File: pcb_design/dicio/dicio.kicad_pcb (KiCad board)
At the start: 2 copper layers, 93 x 93 mm, 88 parts, among them J1 USB_OTG, J2 Conn_01x06_Female, J3 Screw_Terminal_01x06, J4 Screw_Terminal_01x11, J5 Conn_02x03_Odd_Even, J6 Screw_Terminal_01x05, J7 Screw_Terminal_01x09, P1 USB_C_Plug_USB2.0, SW1 SW_SPST, SW2 SW_SPST, SW3 SW_DIP_x08, U1 FT232RL, U2 MCP2542FD, U3 dsPIC33EP512MC806, U4 TPS737, U5 PCA9670, U6 TPS61040, U7 RP604x, U8 gloxinia_connector_small, Y1 Crystal_GND24

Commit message: New dicio design.
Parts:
- removed C28: 10uF, Capacitor_SMD:C_1210_3225Metric
- removed D3, D5: LED, LED_SMD:LED_0603_1608Metric
- removed D6: MBR0530, Diode_SMD:D_SOD-123
- removed H1, H2, H3, H4: MountingHole, MountingHole:MountingHole_3.2mm_M3
- removed JP1: Jumper_NC_Small, Jumper:SolderJumper-2_P1.3mm_Open_RoundedPad1.0x1.5mm
- removed JP2: Jumper, Jumper:SolderJumper-2_P1.3mm_Open_RoundedPad1.0x1.5mm
- removed L1: 10uH, custom_footprints:L_6.5mmx4.5mm_Bourns
- removed L2: 2.2uH, custom_footprints:L_L4mm_D4mm_H1.8mm
- removed P1: USB_C_Plug_USB2.0, custom_footprints:USB_C_Receptacle_Amphenol_12401832E402A
- removed R16: 1.8M, Capacitor_SMD:C_0603_1608Metric
- removed R17: 205k, Capacitor_SMD:C_0603_1608Metric
- removed R21, R23: 4.9k, Resistor_SMD:R_0603_1608Metric
- removed SW3: SW_DIP_x08, Button_Switch_SMD:SW_DIP_SPSTx08_Slide_Omron_A6H-8101_W6.15mm_P1.27mm
- removed U8: gloxinia_connector_small, Connector_PinHeader_2.54mm:PinHeader_2x13_P2.54mm_Vertical
- added C29: 20pF, Capacitor_SMD:C_0603_1608Metric, F.Cu at (73.1, 75.2)
- added C30: 4.7nF, Capacitor_SMD:C_0603_1608Metric, F.Cu at (101.2, 53.7)
- added C31: 0.1uF, Capacitor_SMD:C_0603_1608Metric, F.Cu at (105.2, 82.8)
- added C32: 0.1uF, Capacitor_SMD:C_0603_1608Metric, F.Cu at (67.6, 85.5)
- added J8: USB_C_Receptacle, custom_footprints:USB_C_Receptacle_Amphenol_12401861XX12A, F.Cu at (107.5, 127.9)
- added Q1: Q_NMOS_GSD, Package_TO_SOT_SMD:SOT-23, F.Cu at (97.6, 54.5)
- added Y2: Crystal_GND24, Crystal:Crystal_SMD_Abracon_ABM3B-4Pin_5.0x3.2mm, F.Cu at (86.0, 72.3)
- C16: value 10uF -> 1uF; footprint Capacitor_SMD:C_1210_3225Metric -> Capacitor_SMD:C_0603_1608Metric
- C17: value 4.7pF -> 1uF
- C18: value 1uF -> 0.1uF; footprint Capacitor_SMD:C_1206_3216Metric -> Capacitor_SMD:C_0603_1608Metric
- C19, C27: value 10uF -> 0.1uF; footprint Capacitor_SMD:C_1210_3225Metric -> Capacitor_SMD:C_0603_1608Metric
- C20: value 10uF -> 1nF; footprint Capacitor_SMD:C_1210_3225Metric -> Capacitor_SMD:C_0603_1608Metric
- C21, C22: value 22uF -> 4.7uF; footprint Capacitor_SMD:C_1210_3225Metric -> Capacitor_SMD:C_1206_3216Metric
- C23: footprint Capacitor_SMD:C_1210_3225Metric -> Capacitor_SMD:C_1206_3216Metric
- C6: value 10uF -> 20pF; footprint Capacitor_SMD:C_1210_3225Metric -> Capacitor_SMD:C_0603_1608Metric
- C7, C8: value 10pF -> 20pF
- J1: value USB_OTG -> Conn_02x03_Counter_Clockwise; footprint Connector_USB:USB_Micro-B_Molex-105017-0001 -> Connector_PinSocket_2.54mm:PinSocket_2x03_P2.54mm_Vertical
- J3: value Screw_Terminal_01x06 -> USB_C_Receptacle; footprint custom_footprints:TB003-500-06 -> custom_footprints:USB_C_Receptacle_Amphenol_12401861XX12A
- J4: value Screw_Terminal_01x11 -> Micro_SD_Card; footprint custom_footprints:TB003-500-11 -> Connector_Card:microSD_HC_Wuerth_693072010801
- J5: value Conn_02x03_Odd_Even -> USB_C_Receptacle; footprint Connector_PinHeader_2.54mm:PinHeader_2x03_P2.54mm_Vertical -> custom_footprints:USB_C_Receptacle_Amphenol_12401861XX12A
- J6: value Screw_Terminal_01x05 -> USB_C_Receptacle; footprint custom_footprints:TB003-500-05 -> custom_footprints:USB_C_Receptacle_Amphenol_12401861XX12A
- J7: value Screw_Terminal_01x09 -> Conn_02x13_Odd_Even; footprint custom_footprints:TB003-500-06 -> Connector_PinHeader_2.54mm:PinHeader_2x13_P2.54mm_Vertical
- N1: footprint custom_footprints:Enclosure-Hammond-1554LA -> custom_footprints:Enclosure-Gloxinia2
- R1: value 10k -> 1k
- R11: value 120 -> 1M
- R18: value 120R -> 60R; footprint Resistor_THT:R_Axial_DIN0204_L3.6mm_D1.6mm_P7.62mm_Horizontal -> Resistor_SMD:R_0603_1608Metric
- R4, R9: value 750 -> 100k
- R7: value 1M -> 60R
- SW1, SW2: footprint Button_Switch_SMD:SW_SPST_KMR2 -> Button_Switch_SMD:SW_Push_1P1T_NO_CK_KMR2
- U1: value FT232RL -> dsPIC33EP256MU806; footprint Package_SO:SSOP-28_5.3x10.2mm_P0.65mm -> Package_QFP:TQFP-64_10x10mm_P0.5mm
- U3: value dsPIC33EP512MC806 -> S70FL01GS; footprint Package_QFP:TQFP-64_10x10mm_P0.5mm -> custom_footprints:SOIC-16_25.75x18.75mm_P2.5mm; moved to B.Cu
- U5: value PCA9670 -> SiP32431; footprint Package_SO:TSSOP-16_4.4x5mm_P0.65mm -> Package_TO_SOT_SMD:SOT-363_SC-70-6
- U6: value TPS61040 -> SiP32431; footprint Package_TO_SOT_SMD:SOT-23-5 -> Package_TO_SOT_SMD:SOT-363_SC-70-6
- U7: value RP604x -> ADM7170; footprint custom_footprints:DFN_12_Pin_2.7x3mm_P0.5mm -> Package_CSP:LFCSP-8-1EP_3x3mm_P0.5mm_EP1.45x1.74mm
- moved J7 85.2 mm to (70.0, 45.0), turned to 90 degrees
- moved J3 84.9 mm to (62.5, 127.9)
- moved C4 80.4 mm to (52.0, 50.8), turned to 90 degrees
- moved R6 79.9 mm to (51.3, 53.5)
- moved SW2 78.0 mm to (56.0, 50.8), turned to 0 degrees
- moved J2 70.1 mm to (55.0, 56.0)
- moved R2 65.7 mm to (61.2, 51.0), turned to -90 degrees
- moved C3 64.8 mm to (62.9, 50.9), turned to 90 degrees
- moved SW1 63.0 mm to (66.6, 51.0), turned to 0 degrees
- moved U5 59.6 mm to (119.5, 96.8)
- moved J6 56.6 mm to (77.5, 127.9), turned to 0 degrees
- moved R7 55.2 mm to (99.4, 49.5), turned to 0 degrees
- moved R4 54.3 mm to (69.6, 75.5), turned to 0 degrees
- moved R12 52.6 mm to (106.7, 76.2)
- moved R18 50.4 mm to (99.4, 51.1), turned to 180 degrees
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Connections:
- net /~MCLR renamed /~{MCLR}
- C12 pad 1: +3V3 -> GND
- C12 pad 2: GND -> +3V3
- C13 pad 2: +3V3 -> VDDA
- C14 pad 1: +3V3 -> GND
- C14 pad 2: GND -> +3V3
- C16 pad 1: VBUS -> +3V3
- C17 pad 1: +12V -> VDDA
- C17 pad 2: Net-(C17-Pad2) -> GND
- C18 pad 1: +12V -> /S_PS
- C19 pad 1: VBUS -> /S_PS
- C2 pad 1: GND -> +3V3
- C2 pad 2: Net-(C2-Pad2) -> GND
- C20 pad 1: VBUS -> Net-(C20-Pad1)
- C21 pad 1: +5V -> VDDA
- C22 pad 1: +5V -> VBUS
- C23 pad 1: +3V3 -> /VCAP
- C27 pad 1: +12V -> +3V3
- C3 pad 1: Net-(C3-Pad1) -> /BTN
- C6 pad 1: Net-(C6-Pad1) -> GND
- C6 pad 2: GND -> /SOSC1
- C7 pad 2: Net-(C7-Pad2) -> /OSC2
- C8 pad 2: /CLK_IN -> /OSC1
- J1 pad 1: /V_USBC -> +3V3
- J1 pad 2: /D- -> /U1RX
- J1 pad 3: /D+ -> /~{U1RTS}
- J1 pad 4: Net-(J1-Pad4) -> /~{U1CTS}
- J1 pad 5: GND -> /U1TX
- J2 pad 6: /PGM -> unconnected-(J2-Pad6)
- J4 pad 1: GND -> unconnected-(J4-Pad1)
- J4 pad 2: /SCK2 -> /~{CS_SD}
- J4 pad 3: /SDO2 -> /MOSI1
- J4 pad 4: /SDI2 -> +3V3
- J4 pad 5: /~CS2_1 -> /SCK1
- J4 pad 6: /~CS2_2 -> GND
- J4 pad 7: +3V3 -> /MISO1
- J4 pad 8: /~INT2 -> unconnected-(J4-Pad8)
- J4 pad 9: /SDA2 -> GND
- J7 pad 1: +3V3 -> VBUS
- J7 pad 2: /U1RX -> VBUS
- J7 pad 3: /U1TX -> /V_USBC
- J7 pad 4: /~U1RTS -> VBUS
- J7 pad 5: /~U1CTS -> /CAN_H
- J7 pad 6: GND -> /V_USBC
- R1 pad 1: /~RST_FTDI -> Net-(Q1-Pad1)
- R1 pad 2: VBUS -> /TERM
- R10 pad 1: Net-(R10-Pad1) -> /~{MCLR_w}
- R11 pad 1: /CAN_L -> /OSC2
- R11 pad 2: /CAN_H -> /OSC1
- R18 pad 1: /CAN_L -> Net-(C30-Pad1)
- R18 pad 2: /CAN_H -> Net-(Q1-Pad2)
- R19 pad 1: Net-(P1-PadA5) -> /VCONN
- R2 pad 2: Net-(C3-Pad1) -> /BTN
- R20 pad 2: Net-(P1-PadB5) -> /CC1
- R22 pad 2: /~INT1 -> /~{INT1}
- R24 pad 2: /~INT2 -> /~{INT2}
- R4 pad 1: /BLINK -> +3V3
- R4 pad 2: Net-(D3-Pad2) -> /~{SQICS1}
- R7 pad 1: Net-(C7-Pad2) -> /CAN_L
- R7 pad 2: /CLK_IN -> Net-(C30-Pad1)
- R9 pad 1: Net-(R9-Pad1) -> +3V3
- R9 pad 2: Net-(D5-Pad2) -> /~{SQICS0}
- SW1 pad 2: Net-(C3-Pad1) -> /BTN
- U1 pad 1: /MCU_RXD -> /~{U1RTS}
- U1 pad 10: Net-(U1-Pad10) -> +3V3
- U1 pad 11: /MCU_~RTS -> /S_PS_SW
- U1 pad 12: Net-(U1-Pad12) -> /~{INT1}
- U1 pad 13: Net-(U1-Pad13) -> /OW2
- U1 pad 14: Net-(U1-Pad14) -> /AS2
- U1 pad 15: /D+ -> /OW4
- U1 pad 16: /D- -> /AS4
- U1 pad 17: Net-(C2-Pad2) -> /PGC
- U1 pad 18: GND -> /PGD
- U1 pad 19: /~RST_FTDI -> VDDA
- U1 pad 2: Net-(U1-Pad2) -> /OW1
- U1 pad 20: +5V -> GND
- U1 pad 21: GND -> /EN_VA
- U1 pad 22: Net-(U1-Pad22) -> /SYNC
- U1 pad 23: Net-(R9-Pad1) -> /CAN_C2
- U1 pad 24: (no net) -> /CAN_C1
- U1 pad 26: GND -> +3V3
- U1 pad 27: Net-(U1-Pad27) -> /C1TX
- U1 pad 28: Net-(U1-Pad28) -> /C1RX
- U1 pad 3: /MCU_~CTS -> /U1TX
- U1 pad 4: +3V3 -> /OW3
- U1 pad 5: /MCU_TXD -> /~{U1CTS}
- U1 pad 6: Net-(U1-Pad6) -> /U1RX
- U1 pad 7: GND -> /~{MCLR_w}
- U1 pad 8: (no net) -> unconnected-(U1-Pad8)
- U1 pad 9: Net-(U1-Pad9) -> GND
- U3 pad 1: /MCU_~RTS -> /~{HOLD}
- U3 pad 10: +3V3 -> GND
- U3 pad 11: /BLINK -> unconnected-(U3-Pad11)
- U3 pad 12: /ERR -> unconnected-(U3-Pad12)
- U3 pad 13: Net-(U3-Pad13) -> unconnected-(U3-Pad13)
- U3 pad 14: Net-(U3-Pad14) -> +3V3
- U3 pad 15: Net-(U3-Pad15) -> /SI
- U3 pad 16: Net-(U3-Pad16) -> /SQICLK
- U3 pad 2: /MCU_~CTS -> +3V3
- U3 pad 3: /MCU_TXD -> /~{RESET_M}
- U3 pad 4: /SDO2 -> unconnected-(U3-Pad4)
- U3 pad 5: /MCU_RXD -> unconnected-(U3-Pad5)
- U3 pad 6: /SCK2 -> /~{SQICS1}
- U3 pad 7: Net-(R10-Pad1) -> /~{SQICS0}
- U3 pad 8: Net-(U3-Pad8) -> /SO
- U3 pad 9: GND -> /~{WP}
- U5 pad 1: +3V3 -> /S_PS
- U5 pad 2: +3V3 -> GND
- U5 pad 3: +3V3 -> /S_PS_SW
- U5 pad 4: Net-(SW3-Pad16) -> +3V3
- U5 pad 5: Net-(SW3-Pad15) -> GND
- U5 pad 6: Net-(SW3-Pad14) -> unconnected-(U5-Pad6)
- U6 pad 1: Net-(D6-Pad2) -> /S_PS
- U6 pad 3: Net-(C17-Pad2) -> /EN_VA
- U6 pad 4: VBUS -> VDDA
- U6 pad 5: VBUS -> GND
- U7 pad 1: VBUS -> VDDA
- U7 pad 2: VBUS -> VDDA
- U7 pad 3: GND -> VDDA
- U7 pad 4: GND -> Net-(C20-Pad1)
- U7 pad 5: GND -> /EN_VA
- U7 pad 6: +5V -> GND
- U7 pad 7: +5V -> VBUS
- U7 pad 8: Net-(L2-Pad2) -> VBUS
- Y1 pad 1: /CLK_IN -> /SOSC2
- Y1 pad 3: Net-(C7-Pad2) -> /SOSC1
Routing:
- net +3V3: track 606.6 -> 342.9 mm, vias 29 -> 18
- net +5V: track 190.2 -> 0.00 mm, vias 2 -> 0
- net /S_PS: track 0.00 -> 144.3 mm, vias 0 -> 6
- net +12V: track 130.5 -> 0.00 mm, vias 4 -> 0
- net /~{INT1}: track 0.00 -> 121.3 mm, vias 0 -> 6
- net /~{MCLR}: track 134.0 -> 12.8 mm, vias 12 -> 0
- net /~{U1CTS}: track 0.00 -> 107.3 mm, vias 0 -> 4
- net /CLK: track 104.0 -> 0.00 mm, vias 4 -> 0
- net /~{U1RTS}: track 0.00 -> 98.7 mm, vias 0 -> 4
- net /~{INT2}: track 0.00 -> 96.3 mm, vias 0 -> 8
- net /~INT2: track 96.2 -> 0.00 mm, vias 4 -> 0
- net /~RST2: track 88.7 -> 0.00 mm, vias 1 -> 0
- net /U1RX: track 58.7 -> 136.8 mm
- net /~U1RTS: track 71.0 -> 0.00 mm
- net /SDA2: track 79.4 -> 150.2 mm, vias 3 -> 10
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- added copper zone on F.Cu, net /S_PS
- removed copper zone on F.Cu, net +5V
- removed copper zone on F.Cu, net VBUS
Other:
- outline, holes or cut-outs redrawn
- net class Default removed
- board text removed: "12V"
- board text removed: "3.3V"
- board text removed: "5V"
- board text removed: "ACT"
- board text removed: "ADDR"
- board text removed: "BLK"
- board text removed: "BP"
- board text removed: "CH"
- board text removed: "CL"
- board text removed: "CLK"
- board text removed: "CLK IN"
- board text removed: "ERR"
- board text removed: "G IO"
- board text removed: "GND"
- board text removed: "IO"
- board text removed: "PGM"
- board text removed: "PWR"
- board text removed: "RST"
- board text removed: "RX"
- board text removed: "Rev. 4"
- board text removed: "SCK"
- board text removed: "SCL"
- board text removed: "SDA"
- board text removed: "SDI"
- board text removed: "SDO"
- board text removed: "TERM"
- board text removed: "TX"
- board text removed: "USER"
- board text removed: "VB"
- board text removed: "dicio"
- board text removed: "gloxinia system"
- board text removed: "~CS1"
- board text removed: "~CS2"
- board text removed: "~CTS"
- board text removed: "~INT"
- board text removed: "~RST"
- board text removed: "~RTS"

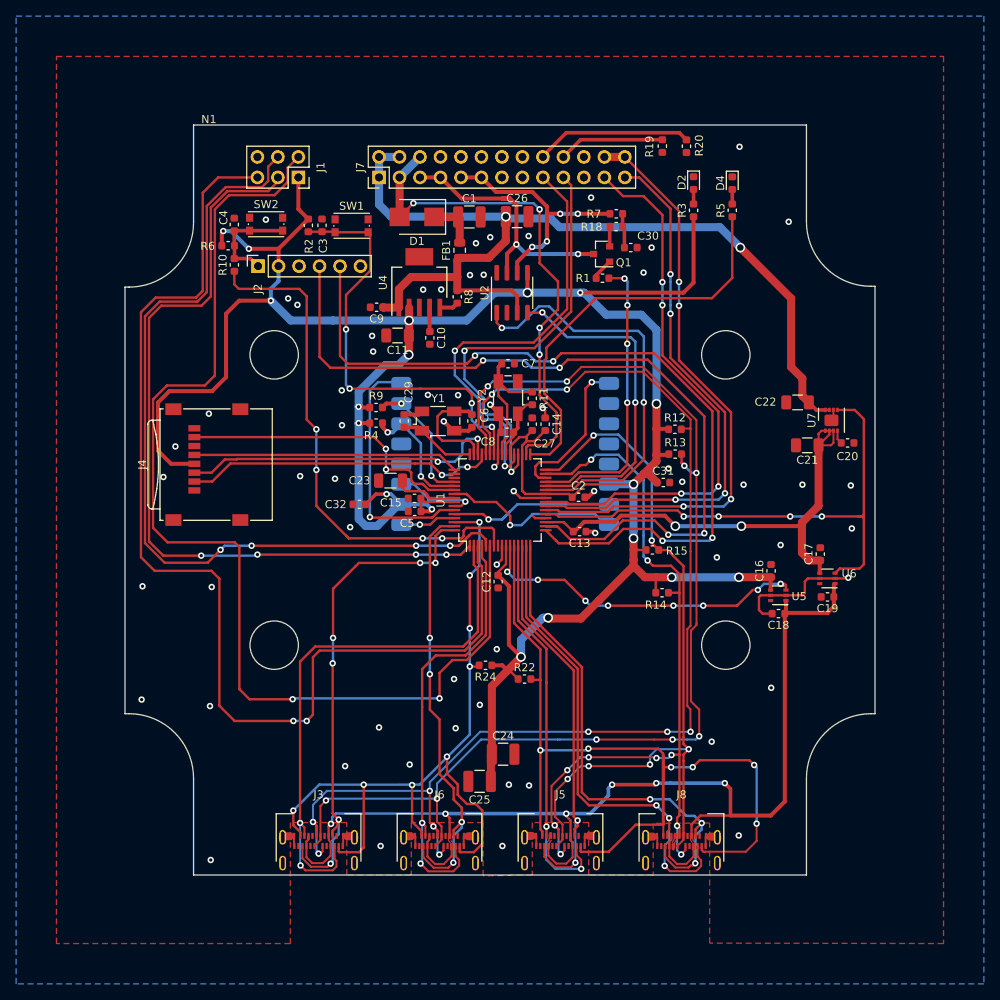
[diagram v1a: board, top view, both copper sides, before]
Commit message: Updated for new mounting hole locations
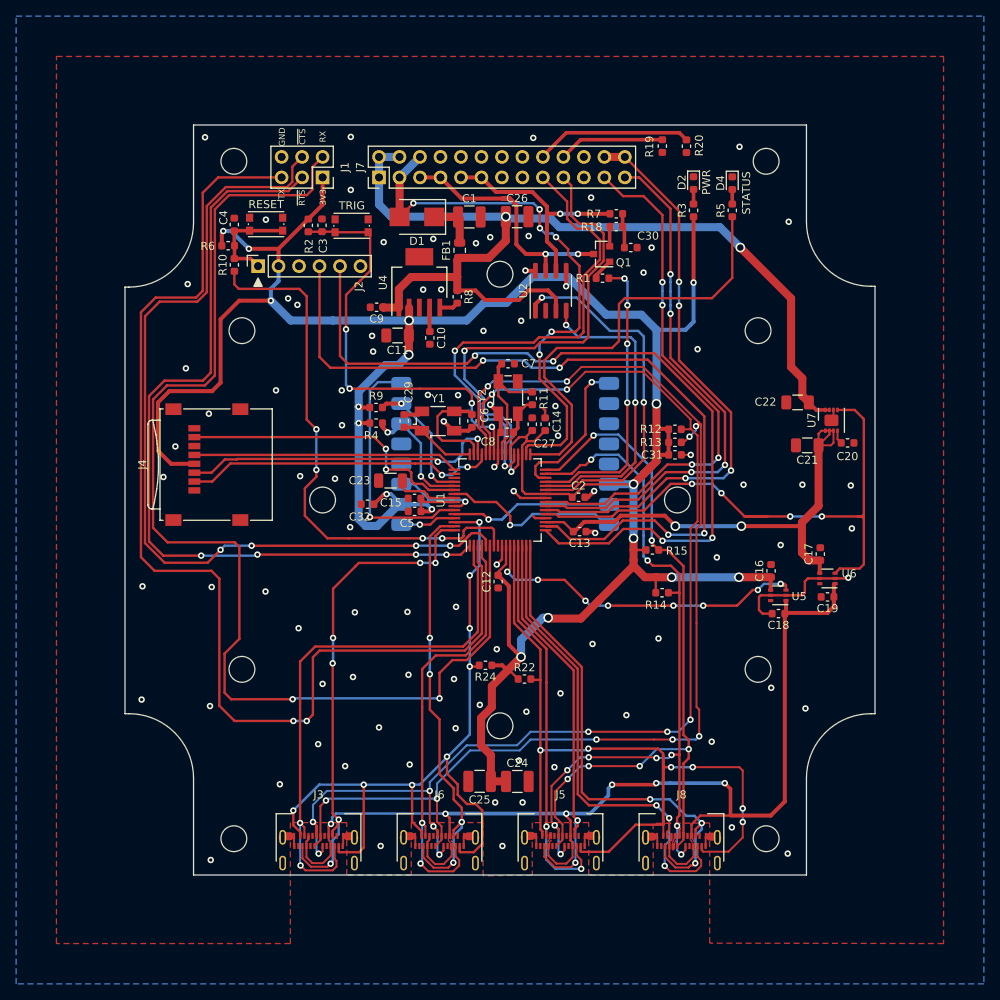
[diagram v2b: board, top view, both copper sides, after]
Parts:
- moved U2 4.81 mm to (91.3, 59.0)
- moved C24 3.81 mm to (87.2, 119.9)
- moved C31 3.72 mm to (106.7, 79.4)
- moved J1 3.00 mm to (63.0, 45.0)
- moved R13 1.46 mm to (106.7, 77.8)
- moved C32 1.02 mm to (68.6, 85.5)
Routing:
- net /D-: track 53.2 -> 60.7 mm
- net /D+: track 54.0 -> 61.1 mm
- net /V_USBC: track 63.0 -> 69.5 mm, vias 4 -> 6
- net /U1RX: track 136.8 -> 143.2 mm
- net /C1TX: track 51.4 -> 45.6 mm
- net /EN_VA: track 66.8 -> 72.4 mm
- net VBUS: track 116.8 -> 122.1 mm
- net /~{INT1}: track 121.3 -> 116.7 mm
- net /C1RX: track 42.4 -> 38.5 mm
- net /ERR: track 51.4 -> 55.1 mm
- net /~{U1CTS}: track 107.3 -> 110.4 mm
- net /U1TX: track 138.5 -> 141.5 mm
- net /~{U1RTS}: track 98.7 -> 101.2 mm
- net GND: track 65.4 -> 67.8 mm, vias 63 -> 93
- net /~{MCLR_w}: track 64.8 -> 67.1 mm
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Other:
- board text added: "3V3"
- board text added: "GND"
- board text added: "PWR"
- board text added: "RESET"
- board text added: "RX"
- board text added: "STATUS"
- board text added: "TRIG"
- board text added: "TX"
- board text added: "~{CTS}"
- board text added: "~{RTS}"

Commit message: Improved design.
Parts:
- moved C31 2.00 mm to (106.7, 77.4)
- moved R12 2.00 mm to (106.7, 74.2)
- moved R13 2.00 mm to (106.7, 75.8)
- moved SW2 1.30 mm to (57.3, 50.8)
- moved D4 0.50 mm to (113.3, 45.7)
- moved R5 0.50 mm to (113.3, 49.1)
- moved C4 0.45 mm to (51.6, 50.9), turned to 0 degrees
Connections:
- U1 pad 27: /C1TX -> unconnected-(U1-Pad27)
- U1 pad 3: /U1TX -> /OW3
- U1 pad 4: /OW3 -> /U1TX
- U1 pad 51: unconnected-(U1-Pad51) -> /C1TX
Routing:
- net /C1TX: track 45.6 -> 55.7 mm
- net /U1TX: track 141.5 -> 147.8 mm, vias 2 -> 4
- net /S_PS: track 144.3 -> 139.2 mm, vias 6 -> 7
- net /~{U1CTS}: track 110.4 -> 114.4 mm, vias 4 -> 6
- net /U1RX: track 143.2 -> 146.6 mm
- net /EN_VA: track 72.4 -> 75.7 mm
- net /~{MCLR}: track 12.8 -> 16.1 mm
- net /SYNC: track 72.1 -> 75.0 mm
- net /CAN_C2: track 66.4 -> 69.3 mm
- net /CAN_C1: track 66.0 -> 68.9 mm
- net /~{MCLR_w}: track 67.1 -> 69.5 mm
- net /TERM: track 36.2 -> 34.3 mm
- net /C1RX: track 38.5 -> 36.6 mm
- net /PGC: track 100.6 -> 102.0 mm
- net GND: track 67.8 -> 66.6 mm, vias 93 -> 92
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
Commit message: Placement update.
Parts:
- moved D2 98.9 mm to (56.1, 129.3), turned to 90 degrees
- moved R3 88.7 mm to (56.1, 120.3), turned to -90 degrees
- moved D4 83.8 mm to (113.9, 129.5), turned to 90 degrees
- moved R5 67.2 mm to (114.1, 116.3), turned to -90 degrees
- moved J4 3.21 mm to (50.8, 78.2), turned to 180 degrees
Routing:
- net /ERR: track 55.1 -> 92.7 mm, vias 0 -> 2
- net +3V3: track 343.8 -> 362.0 mm, vias 18 -> 21
- net Net-(D4-Pad2): track 1.80 -> 13.3 mm
- net Net-(D2-Pad2): track 1.81 -> 7.41 mm
- net /~{CS_SD}: track 38.7 -> 34.5 mm
- net /MISO1: track 37.3 -> 41.5 mm
- net /SYNC: track 75.0 -> 72.6 mm, vias 4 -> 2
- net /MOSI1: track 40.3 -> 38.0 mm
- net /CAN_C2: track 69.3 -> 67.2 mm, vias 4 -> 2
- net /CAN_C1: track 68.9 -> 67.1 mm, vias 4 -> 2
- net /~{INT2}: track 96.3 -> 97.4 mm
- net /SCK1: track 33.0 -> 33.9 mm
- net GND: vias 92 -> 95
- net /TERM: vias 4 -> 2

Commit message: Update.
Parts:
- added C28: 0.1uF, Capacitor_SMD:C_0603_1608Metric, F.Cu at (112.5, 64.5)
- added R16: 10k, Capacitor_SMD:C_0603_1608Metric, F.Cu at (112.5, 61.4)
- added U8: FT232RL, Package_SO:SSOP-28_5.3x10.2mm_P0.65mm, F.Cu at (106.7, 60.2)
- U1: value dsPIC33EP256MU806 -> dsPIC33EP512MC806
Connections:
- C11 pad 1: +3V3 -> +3.3V
- C12 pad 2: +3V3 -> +3.3V
- C14 pad 2: +3V3 -> +3.3V
- C15 pad 1: +3V3 -> +3.3V
- C16 pad 1: +3V3 -> +3.3V
- C2 pad 1: +3V3 -> +3.3V
- C24 pad 1: +3V3 -> +3.3V
- C25 pad 1: +3V3 -> +3.3V
- C27 pad 1: +3V3 -> +3.3V
- C31 pad 1: +3V3 -> +3.3V
- C32 pad 1: +3V3 -> +3.3V
- C5 pad 1: +3V3 -> +3.3V
- J1 pad 1: +3V3 -> +3.3V
- J2 pad 2: +3V3 -> +3.3V
- J3 pad A10: /AS1 -> /SCL2
- J3 pad A3: /OW1 -> /SDA2
- J3 pad A6: /SDA2 -> /OW1
- J3 pad A7: /SCL2 -> /AS1
- J3 pad B10: /AS1 -> /SCL2
- J3 pad B3: /OW1 -> /SDA2
- J3 pad B6: /SDA2 -> /OW1
- J3 pad B7: /SCL2 -> /AS1
- J4 pad 4: +3V3 -> +3.3V
- J5 pad A10: /AS2 -> /SCL1
- J5 pad A3: /OW2 -> /SDA1
- J5 pad A6: /SDA1 -> /OW2
- J5 pad A7: /SCL1 -> /AS2
- J5 pad B10: /AS2 -> /SCL1
- J5 pad B3: /OW2 -> /SDA1
- J5 pad B6: /SDA1 -> /OW2
- J5 pad B7: /SCL1 -> /AS2
- J6 pad A10: /AS3 -> /SCL2
- J6 pad A3: /OW3 -> /SDA2
- J6 pad A6: /SDA2 -> /OW3
- J6 pad A7: /SCL2 -> /AS3
- J6 pad B10: /AS3 -> /SCL2
- J6 pad B3: /OW3 -> /SDA2
- J6 pad B6: /SDA2 -> /OW3
- J6 pad B7: /SCL2 -> /AS3
- J8 pad A10: /AS4 -> /SCL1
- J8 pad A3: /OW4 -> /SDA1
- J8 pad A6: /SDA1 -> /OW4
- J8 pad A7: /SCL1 -> /AS4
- J8 pad B10: /AS4 -> /SCL1
- J8 pad B3: /OW4 -> /SDA1
- J8 pad B6: /SDA1 -> /OW4
- J8 pad B7: /SCL1 -> /AS4
- R12 pad 1: +3V3 -> +3.3V
- R13 pad 1: +3V3 -> +3.3V
- R14 pad 1: +3V3 -> +3.3V
- R15 pad 1: +3V3 -> +3.3V
- R2 pad 1: +3V3 -> +3.3V
- R22 pad 1: +3V3 -> +3.3V
- R24 pad 1: +3V3 -> +3.3V
- R3 pad 1: +3V3 -> +3.3V
- R4 pad 1: +3V3 -> +3.3V
- R6 pad 1: +3V3 -> +3.3V
- R9 pad 1: +3V3 -> +3.3V
- U1 pad 10: +3V3 -> +3.3V
- U1 pad 26: +3V3 -> +3.3V
- U1 pad 27: unconnected-(U1-Pad27) -> /USB_CTS
- U1 pad 33: /ERR -> /USB_RX
- U1 pad 34: /V_USBC -> /USB_TX
- U1 pad 35: +3V3 -> /USB_RTS
- U1 pad 36: /D- -> /ERR
- U1 pad 37: /D+ -> unconnected-(U1-Pad37)
- U1 pad 38: +3V3 -> +3.3V
- U1 pad 57: +3V3 -> +3.3V
- U2 pad 5: +3V3 -> +3.3V
- U3 pad 14: +3V3 -> +3.3V
- U3 pad 2: +3V3 -> +3.3V
- U4 pad 2: +3V3 -> +3.3V
- U5 pad 4: +3V3 -> +3.3V
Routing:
- net +3.3V: track 0.00 -> 365.6 mm, vias 0 -> 22
- net +3V3: track 362.0 -> 0.00 mm, vias 21 -> 0
- net /V_USBC: track 69.5 -> 8.50 mm, vias 6 -> 0
- net /USB_CTS: track 0.00 -> 40.9 mm, vias 0 -> 4
- net /USB_TX: track 0.00 -> 40.1 mm, vias 0 -> 4
- net /USB_RX: track 0.00 -> 39.6 mm
- net /USB_RTS: track 0.00 -> 34.7 mm
- net /SDA1: track 97.8 -> 124.7 mm, vias 10 -> 13
- net /D+: track 61.1 -> 38.1 mm, vias 2 -> 1
- net /D-: track 60.7 -> 38.0 mm, vias 2 -> 0
- net /SCL2: track 147.3 -> 169.3 mm, vias 9 -> 13
- net /SCL1: track 93.5 -> 113.7 mm, vias 6 -> 11
- net GND: track 66.6 -> 85.8 mm, vias 95 -> 94
- net /ERR: track 92.7 -> 108.1 mm, vias 2 -> 6
- net /SDA2: track 149.8 -> 162.9 mm
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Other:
- rule pad_to_mask_clearance: 0.051 -> 0
- board text added: "Gloxinia dicio rev. 7"

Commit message: New and updated board designs.
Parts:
- removed J7: Conn_02x13_Odd_Even, Connector_PinHeader_2.54mm:PinHeader_2x13_P2.54mm_Vertical
- J1: value Conn_02x03_Counter_Clockwise -> Conn_02x10_Odd_Even; footprint Connector_PinSocket_2.54mm:PinSocket_2x03_P2.54mm_Vertical -> samtec:SAMTEC_TMMH-110-01-T-DV; moved to B.Cu
- N1: footprint custom_footprints:Enclosure-Gloxinia2 -> custom_footprints:Enclosure-Gloxinia4
- R16: footprint Capacitor_SMD:C_0603_1608Metric -> Resistor_SMD:R_0603_1608Metric
- moved R20 36.5 mm to (71.7, 43.7), turned to 0 degrees
- moved R19 33.4 mm to (71.7, 41.6), turned to 180 degrees
- moved J1 22.0 mm to (85.0, 45.0), turned to 180 degrees
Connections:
- J1 pad 1: +3.3V -> VBUS
- J1 pad 2: /U1RX -> /~{U1RTS}
- J1 pad 3: /~{U1RTS} -> /CAN_H
- J1 pad 5: /U1TX -> /CAN_L
- J1 pad 6: GND -> /U1TX
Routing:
- net +3.3V: track 365.6 -> 410.1 mm
- net /~{U1RTS}: track 100.3 -> 141.5 mm, vias 4 -> 5
- net /~{U1CTS}: track 114.4 -> 148.8 mm, vias 6 -> 7
- net /U1TX: track 147.8 -> 182.1 mm, vias 4 -> 5
- net /CAN_C2: track 67.2 -> 90.8 mm, vias 2 -> 3
- net VBUS: track 135.5 -> 113.0 mm
- net /U1RX: track 146.6 -> 167.8 mm, vias 2 -> 3
- net /D-: track 38.0 -> 57.3 mm, vias 0 -> 1
- net /CAN_C1: track 67.8 -> 86.1 mm, vias 2 -> 3
- net /D+: track 38.1 -> 55.1 mm
- net /CAN_H: track 31.4 -> 16.0 mm, vias 2 -> 3
- net /SYNC: track 72.6 -> 86.4 mm, vias 2 -> 3
- net /CC1: track 19.5 -> 7.48 mm, vias 0 -> 1
- net /CAN_L: track 28.4 -> 17.5 mm, vias 2 -> 1
- net /VCONN: track 13.2 -> 4.02 mm, vias 0 -> 1
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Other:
- outline, holes or cut-outs redrawn
- board text added: "Gloxinia dicio rev. 8"
- board text removed: "3V3"
- board text removed: "GND"
- board text removed: "Gloxinia dicio rev. 7"
- board text removed: "RX"
- board text removed: "TX"
- board text removed: "~{CTS}"
- board text removed: "~{RTS}"

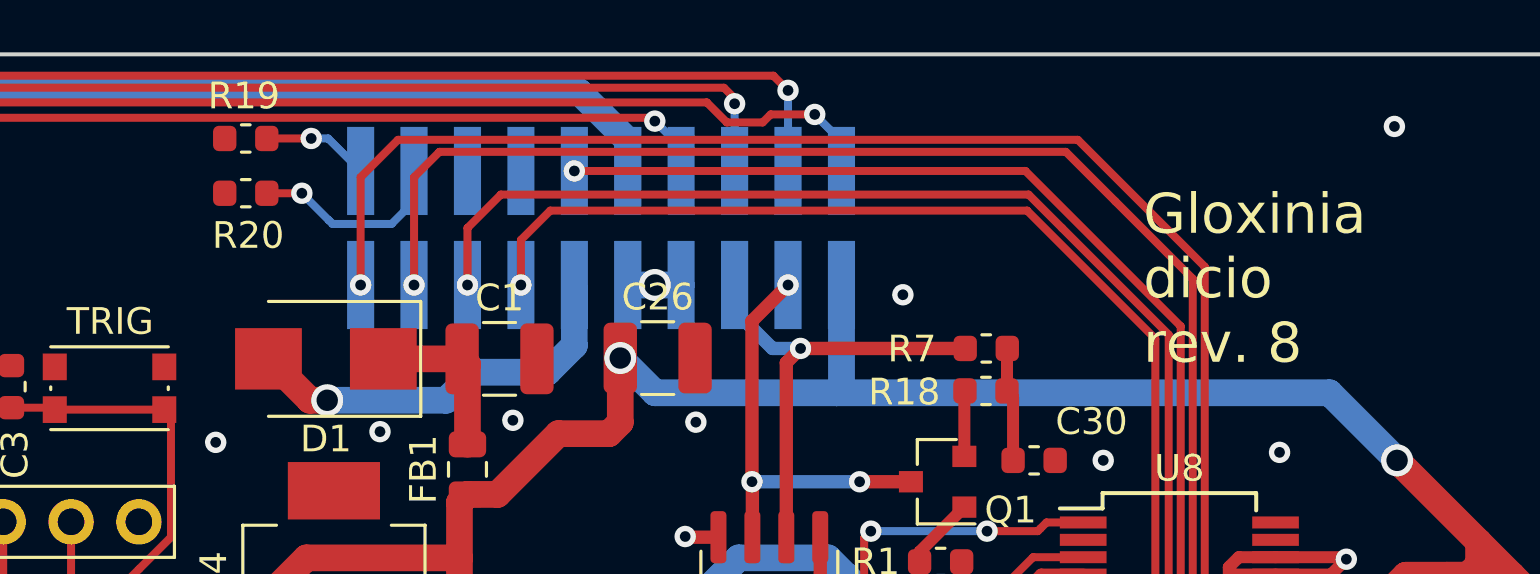
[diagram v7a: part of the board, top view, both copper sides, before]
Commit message: Expose RTCC pin for synchronisation
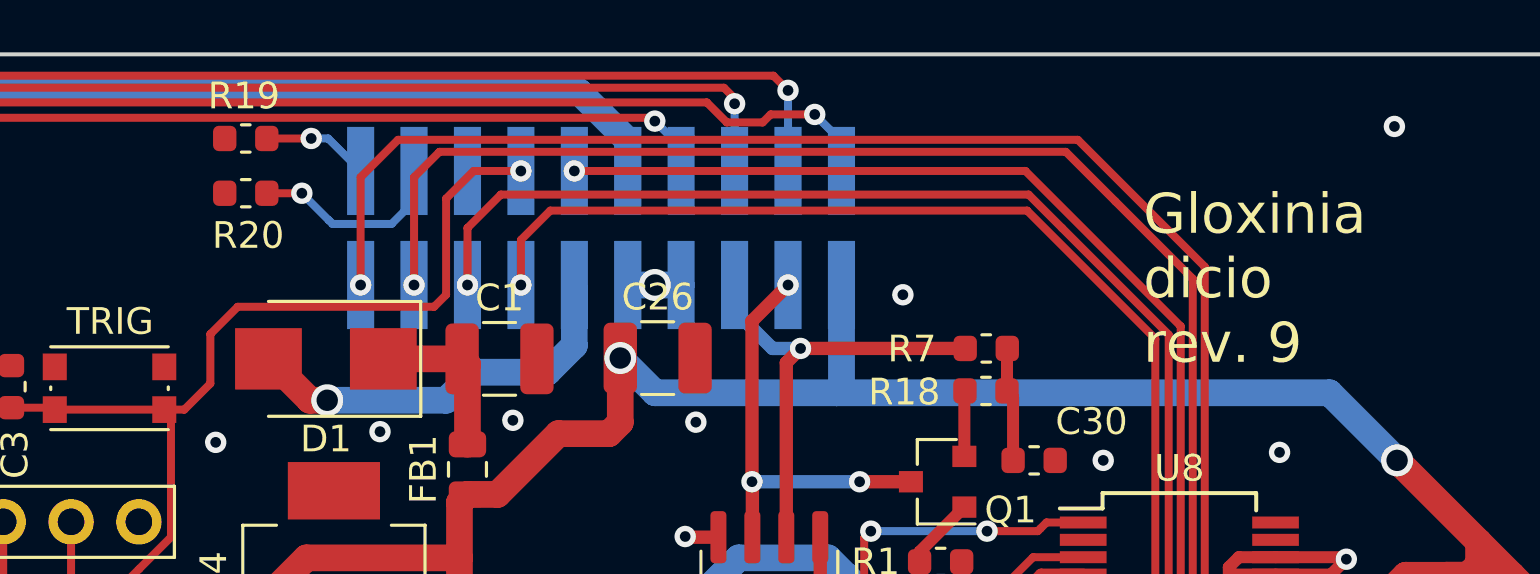
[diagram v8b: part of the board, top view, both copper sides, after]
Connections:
- J1 pad 14: unconnected-(J1-Pad14) -> /BTN
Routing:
- net /BTN: track 53.4 -> 73.6 mm, vias 4 -> 5
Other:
- board text added: "Gloxinia dicio rev. 9"
- board text removed: "Gloxinia dicio rev. 8"
